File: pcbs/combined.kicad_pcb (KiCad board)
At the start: 2 copper layers, 267.6 x 86.8 mm, 108 parts

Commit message: filled zones
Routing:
- added copper zone on B.Cu, net (none)
- added copper zone on F.Cu, net (none)
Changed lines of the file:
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@@
 		(fp_arc
 			(start -4.999998 -2.668498)
-			(mid -4.550008 -2.218496)
+			(mid -4.55001 -2.218496)
 			(end -5 -1.768495)
 			(stroke
@@
 		(fp_arc
 			(start -4.999997 -0.763503)
-			(mid -4.550018 -0.313495)
+			(mid -4.55002 -0.313495)
 			(end -5.000004 0.136506)
 			(stroke
@@
 		(fp_arc
 			(start -1.324995 -6.478502)
-			(mid -0.875006 -6.028496)
+			(mid -0.875008 -6.028496)
 			(end -1.325006 -5.578501)
 			(stroke
@@
 		(net 61)
 	)
+	(zone
+		(net 0)
+		(net_name "")
+		(layers "F&B.Cu")
+		(hatch edge 0.5)
+		(connect_pads
+			(clearance 0.5)
+		)
+		(min_thickness 0.25)
+		(filled_areas_thickness no)
+		(fill yes
+			(thermal_gap 0.5)
+			(thermal_bridge_width 0.5)
+			(island_removal_mode 1)
+			(island_area_min 10)
+		)
+		(polygon
+			(pts
+				(xy 69.59 -1.31) (xy 67.21 144.53) (xy 378.93 151.33) (xy 377.23 -10.48) (xy 69.57 -1.33)
+			)
+		)
+	)
 )

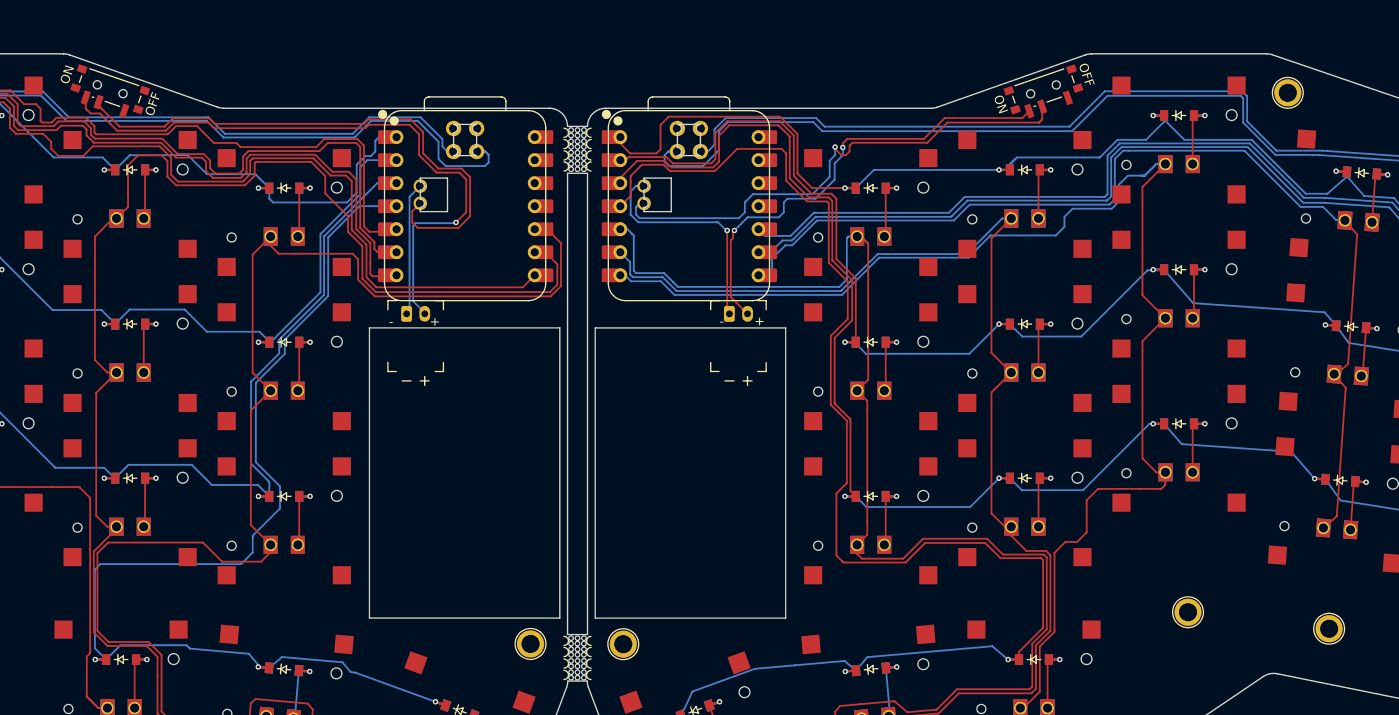
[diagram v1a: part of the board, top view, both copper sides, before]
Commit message: minor changes to the pcb mounting holes, to achieve better symmetry
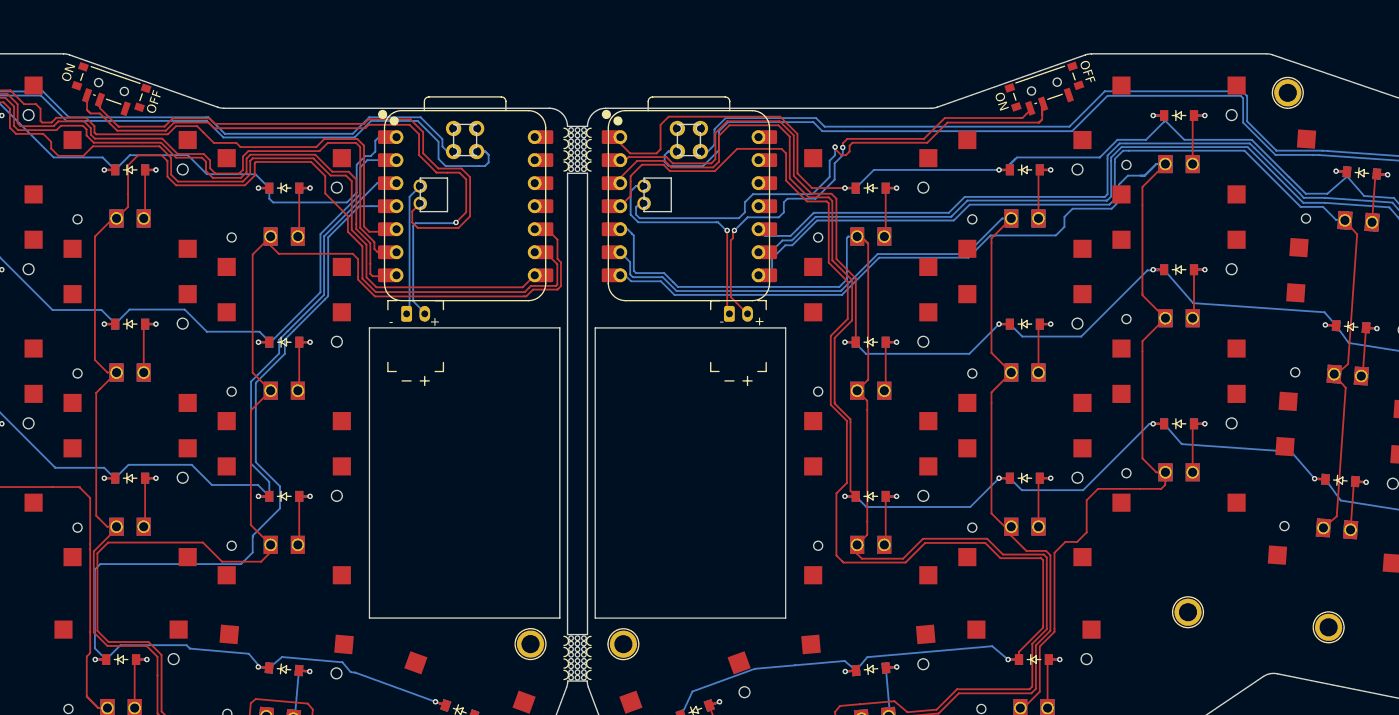
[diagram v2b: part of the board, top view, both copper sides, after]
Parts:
- moved PWR1 0.32 mm to (270.0, 35.7)
- moved PWR1 0.28 mm to (167.1, 35.8)
- moved REF** 0.17 mm to (301.4, 95.3)
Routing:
- net RAW: track 120.1 -> 121.5 mm
- net BAT_P: track 120.4 -> 121.3 mm
